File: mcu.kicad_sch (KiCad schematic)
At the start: 25 parts, among them J301 GPIO, J302 FAN, Q301 AO3400A, SW301 BOOT0, SW302 RST, U301 STM32G0B1KBUx

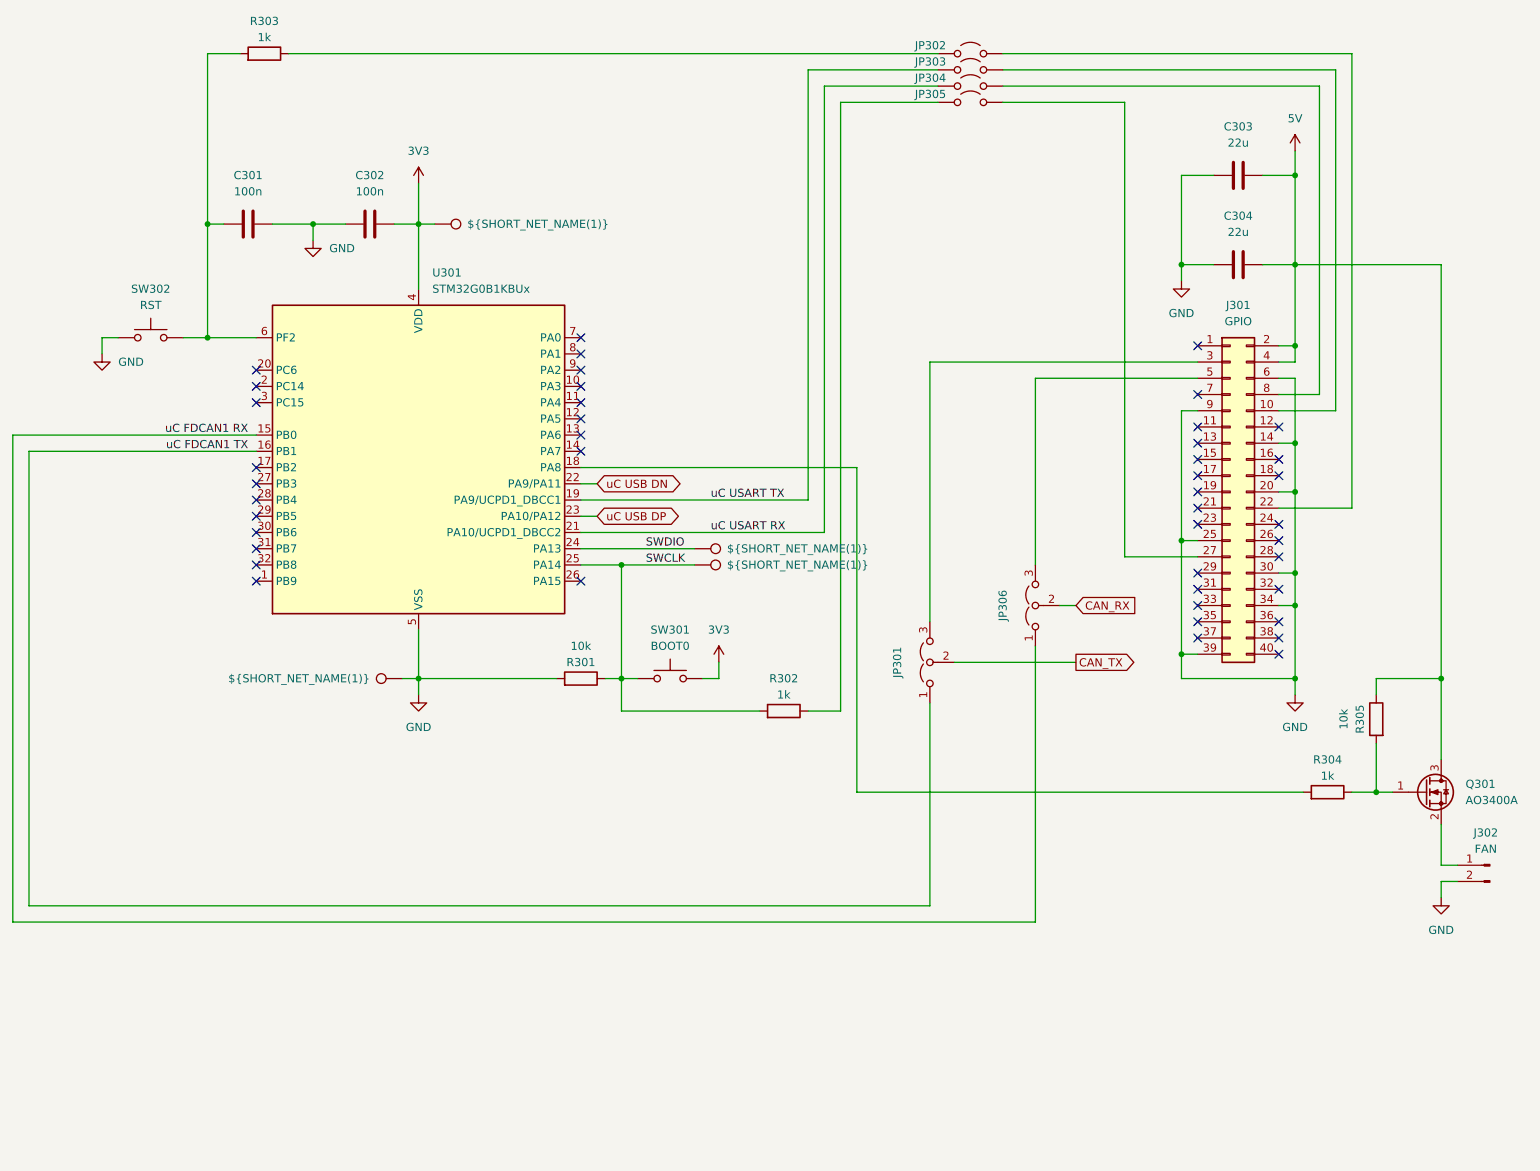
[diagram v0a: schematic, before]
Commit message: Major hardware update: toolhead switching, DC/DC protection, and documentation overhaul
Hardware Changes:
- Replaced reverse polarity protection with 2x PFET toolhead switching (PB2/PA5 control)
- Added SS56 Schottky diode reverse polarity protection for DC/DC converter
- Updated current limit resistor to 5.1kΩ (~10.2A)
- Removed fan control circuitry and JST-XH connector
- Removed internal JST-XH USB port with fuse/protection

Documentation Updates:
- Updated both README files to reflect hardware changes
- Removed all fan control references and configurations
- Updated Klipper configuration examples
- Cleaned up pinout and connector assignments
- Updated technical specifications table
- Fixed table of contents and cross-references
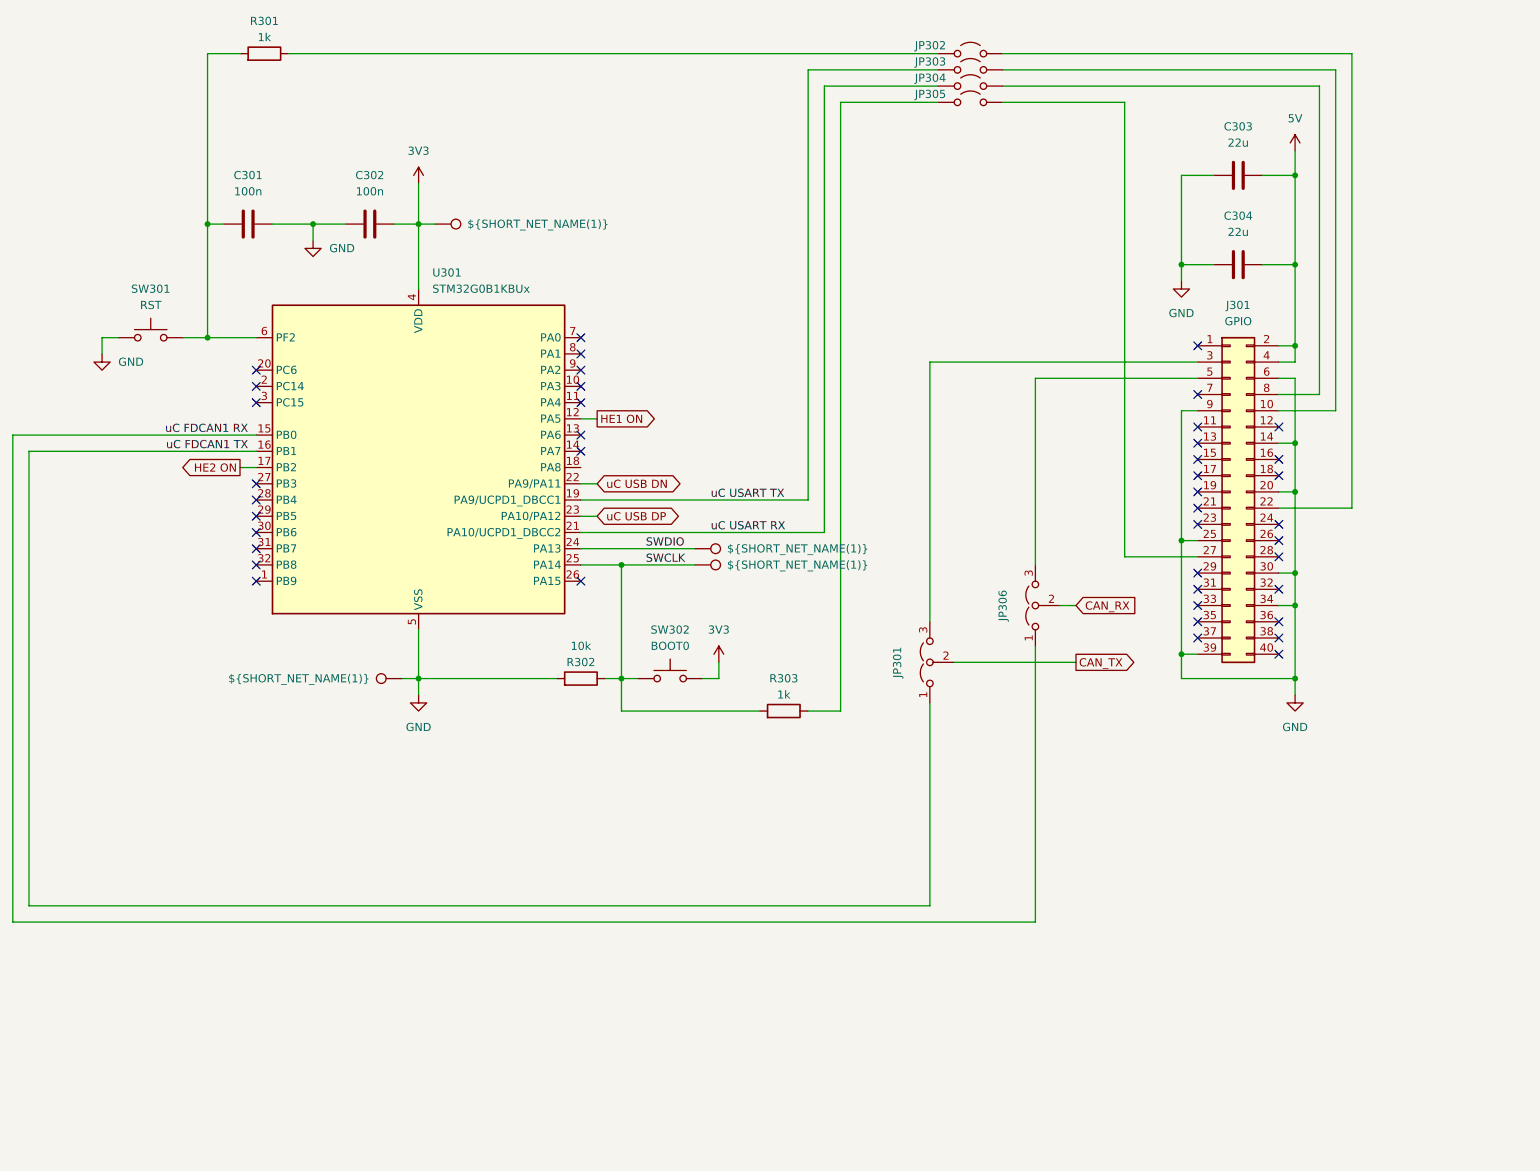
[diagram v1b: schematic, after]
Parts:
- removed J302: FAN, Connector_JST:JST_XH_B2B-XH-A_1x02_P2.50mm_Vertical, symbol Connector:Conn_01x02_Pin
- removed Q301: AO3400A, Package_TO_SOT_SMD:SOT-23, symbol Transistor_FET:AO3400A
- removed R304: 1k, Resistor_SMD:R_0402_1005Metric, symbol Device:R
- removed R305: 10k, Resistor_SMD:R_0402_1005Metric, symbol Device:R
- renumbered R303 to R301, R301 to R302, R302 to R303, SW302 to SW301, SW301 to SW302, TP302 to TP301, TP301 to TP302
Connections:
- net HE1 ON: now reaches U301.12 (PA5)
- net HE2 ON: now reaches U301.17 (PB2)
- no-connect marks 44 -> 42
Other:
- company: (none) -> Eduard Iten
- title: (none) -> EWS - Power, CANbus and USB HAT for 3D Printers

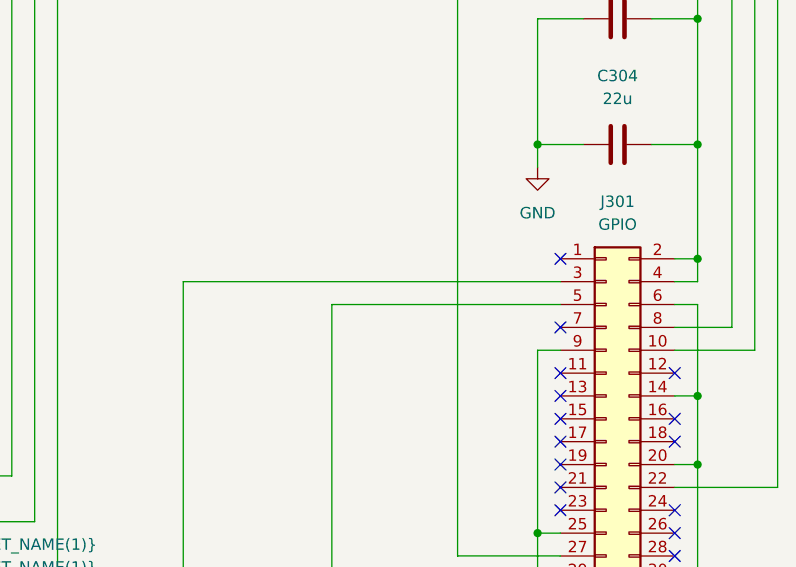
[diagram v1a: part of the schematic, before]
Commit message: Enhanced documentation and final hardware corrections
Documentation Improvements:
- Added comprehensive 'Problems Addressed' section explaining the value proposition
- Covers power supply issues, CAN communication problems, safety concerns, and wiring challenges
- Removed JST-XH internal USB port references from pinout sections
- Corrected via placement specification (DC/DC PGND instead of output)

Hardware Updates:
- Updated schema files with latest component changes
- Added custom footprints for XR76203ELTR-F and heat sink components
- Refined manufacturing guidelines for optimal thermal performance

The documentation now clearly articulates the EWS board's role in solving common
Voron 3D printer control system challenges.
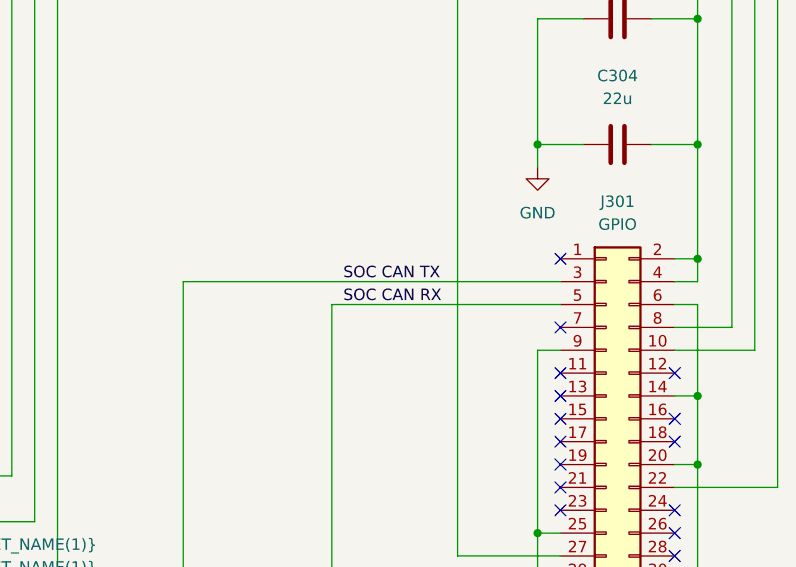
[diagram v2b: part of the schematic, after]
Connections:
- net SOC CAN RX: now reaches J301.5 (Pin_5), JP306.3 (B)
- net SOC CAN TX: now reaches J301.3 (Pin_3), JP301.3 (B)
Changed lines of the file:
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@@
 	(title_block
 		(title "EWS - Power, CANbus and USB HAT for 3D Printers")
-		(date "2025-12-03")
-		(rev "1.0")
+		(date "2025-12-04")
+		(rev "0.1")
 		(company "Eduard Iten")
 	)
@@
 			(width 0)
 			(type default)
+		)
+	)
+	(label "SOC CAN TX"
+		(at 200.66 71.12 0)
+		(effects
+			(font
+				(size 1.27 1.27)
+			)
+			(justify left bottom)
 		)
 	)
@@
 		)
 	)
+	(label "SOC CAN RX"
+		(at 200.66 73.66 0)
+		(effects
+			(font
+				(size 1.27 1.27)
+			)
+			(justify left bottom)
+		)
+	)

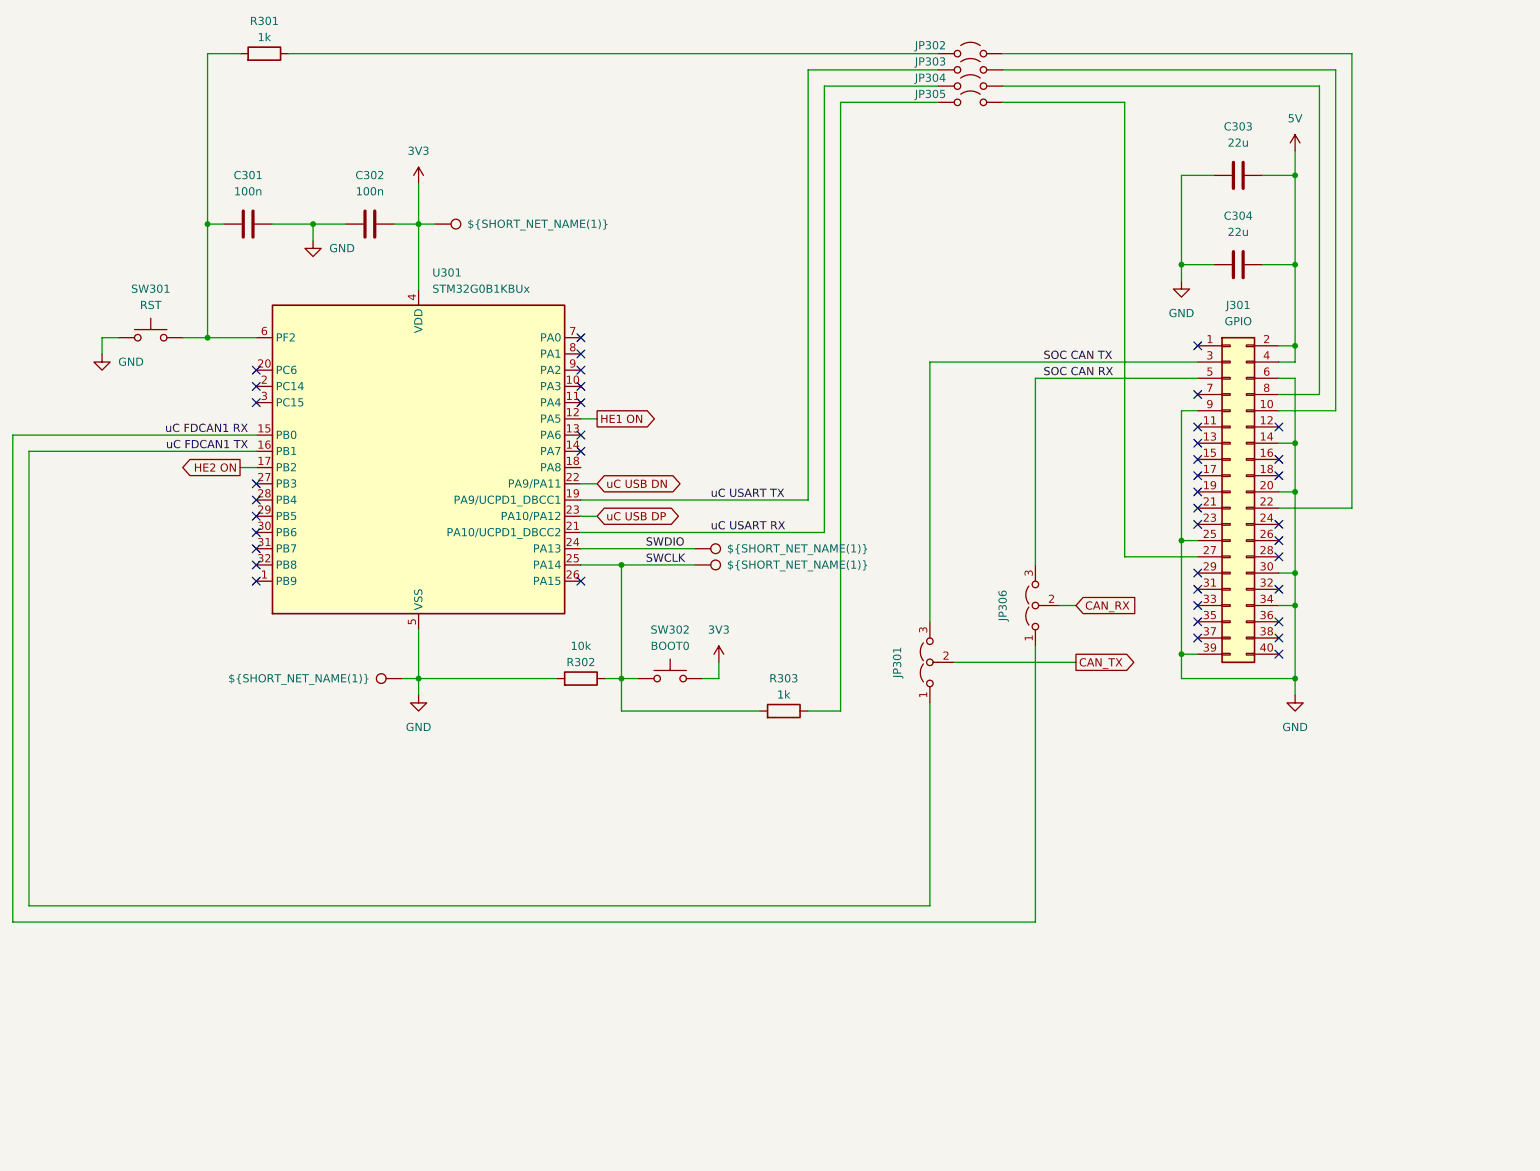
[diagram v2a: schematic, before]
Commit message: EWS Rev 0.1 - Complete design with documentation
Release Features:
- Universal HAT for Raspberry Pi 4/5 and Radxa Rock 5B/5B+
- 8A DC/DC converter with SS56 reverse polarity protection
- Dual toolhead switching via PFETs (PB2/PA5 control)
- Native CAN and USB-CAN bridge support
- USB hub with power delivery for touchscreens
- Comprehensive safety features and thermal management

Hardware:
- STM32G0B1KBU6 MCU with crystal-less design
- MaxLinear XR76208 switching regulator
- MCP2542WFD CAN transceiver with jumper selection
- WCH CH334F USB hub with MTT support
- 2oz copper PCB recommended for thermal performance

Documentation:
- Bilingual documentation (German/English)
- Installation guides with kernel diagnostics
- Klipper configuration examples
- Comprehensive problem statement and solutions
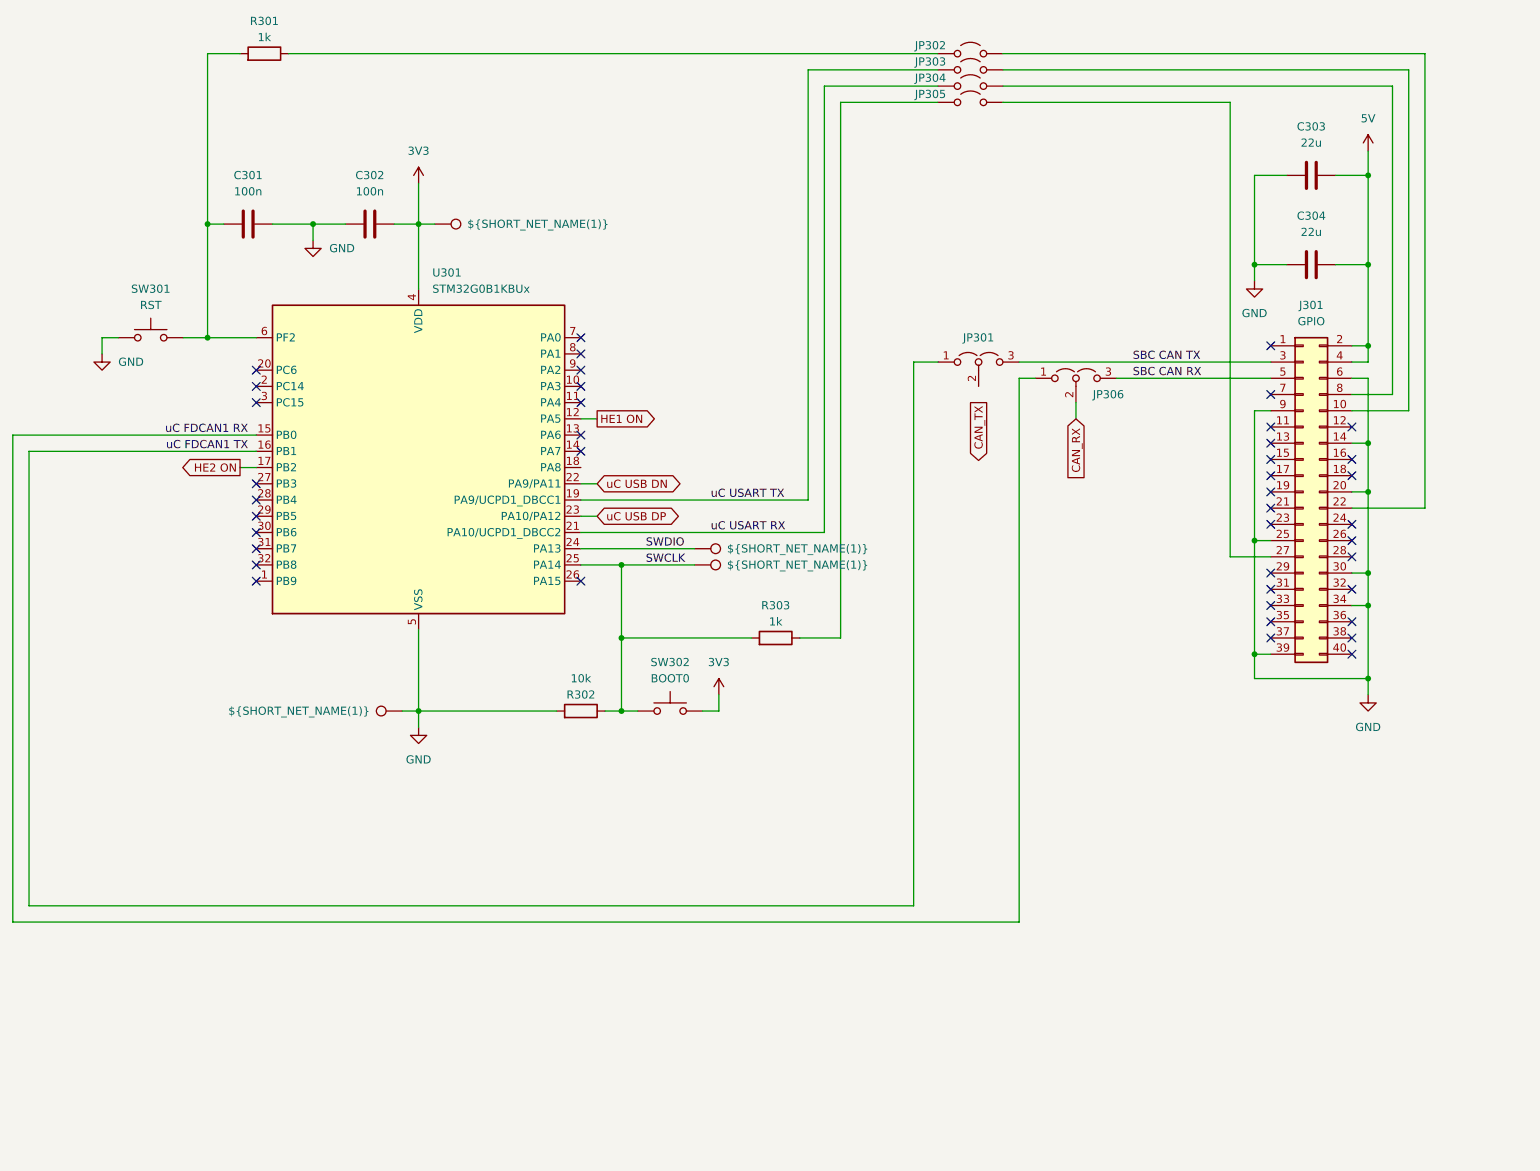
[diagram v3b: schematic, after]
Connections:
- net CAN_TX: no longer JP301.2 (C)
- net SOC CAN RX renamed SBC CAN RX
- net SOC CAN TX renamed SBC CAN TX
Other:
- moved on the sheet: C303, C304, J301, JP301, JP306, R302, R303, SW302
